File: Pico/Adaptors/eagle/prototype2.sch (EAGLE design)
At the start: 13 parts, among them J1 JST-2P-SMD-PW-3410050P1

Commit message: a full panel
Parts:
- added JP12, JP13, JP14: (no value), pinhead-2:PINHD-1X09_2.54-S
- JP1, JP10, JP11, JP2, JP5, JP6, JP7, JP8, JP9: device pinhead-2:PINHD-1X08_2.54-S -> pinhead-2:PINHD-1X09_2.54-S
- U$1: value ESPRUINO_PICO_SMD -> ESPRUINO_PICO_0.1; device espruino_pico:ESPRUINO_PICO_SMD -> espruino_pico:ESPRUINO_PICO_0.1
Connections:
- removed net N$1: JP2.2, U$1.A3
- removed net N$2: JP2.3, U$1.A2
- removed net N$24: JP2.1, U$1.A4
- removed net N$3: JP2.4, U$1.A1
- removed net N$4: JP2.5, U$1.A0
- removed net N$5: JP2.6, U$1.A10
- removed net N$6: JP2.7, U$1.B9
- removed net N$9: JP2.8, U$1.B8
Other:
- moved on the sheet: J1

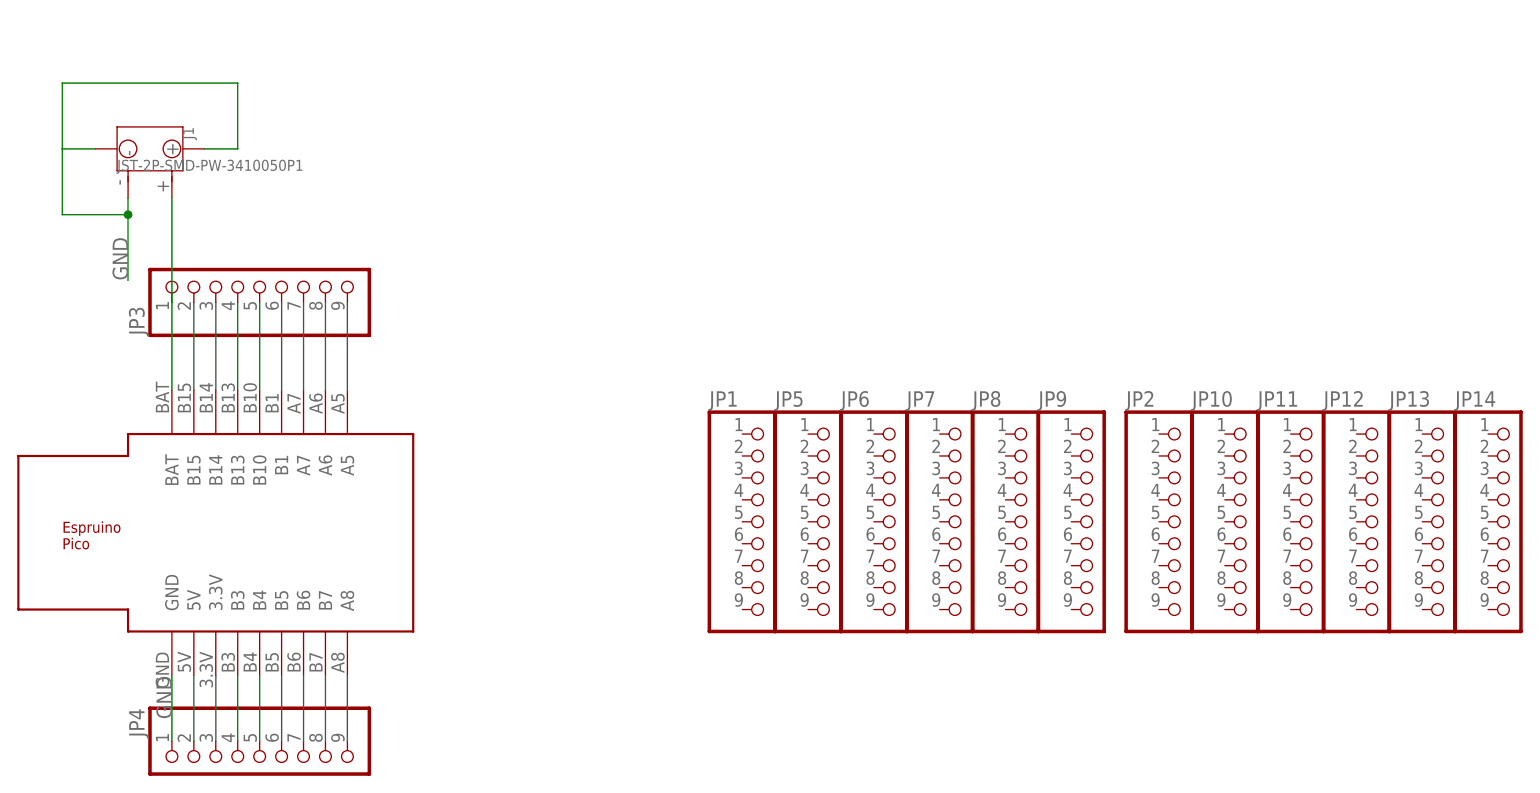
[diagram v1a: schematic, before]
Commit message: Added battery charger pads to proto headers
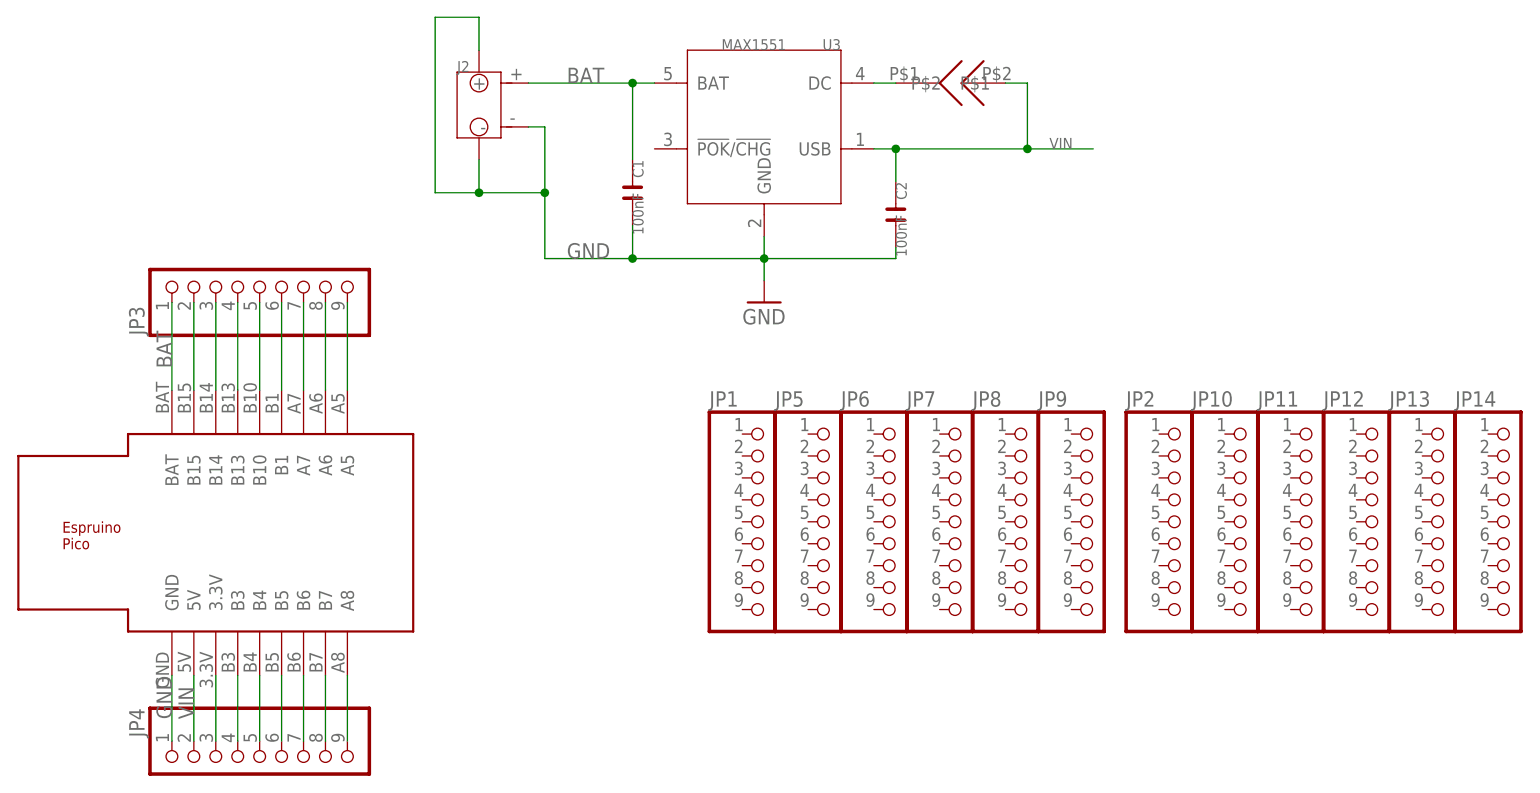
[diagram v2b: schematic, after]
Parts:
- removed J1: JST-2P-SMD-PW-3410050P1, OPL Eagle Library:JST-2P-SMD-PW-3410050P1
- added C1, C2: 100nF, OPL5:C-0603
- added J2: JST-2P-SMD-PW-3410050P1, OPL Eagle Library:JST-2P-SMD-PW-3410050P1
- added U$4: SOLDERJUMPER, solder_jumper:SOLDERJUMPER
- added U3: MAX1551, template:MAX1551
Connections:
- removed net 5V: JP4.2, U$1.5V
- removed net N$15: J1.+, JP3.1, U$1.BAT
- new net BAT: C1.1, J2.+, JP3.1, U$1.BAT, U3.BAT
- new net N$2: U$4.P$1, U3.DC
- new net VIN: C2.1, JP4.2, U$1.5V, U$4.P$2, U3.USB
- net GND: now also C1.2, C2.2, J2.-, J2.3, J2.4, U3.GND; no longer J1.-, J1.3, J1.4
